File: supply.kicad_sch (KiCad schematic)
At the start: 149 parts, among them IC1 TPS54561, J3 DC_SOCKET, J8 61300311121, Q11 DTC014TEBTL, Q12 DTC014TEBTL, Q13 DTC014TEBTL, U10 LM3881MME_NOPB, U12 AP62301WU-7, U17 SN74LVC1G07DBVRG4, U18 MAX812REUS+T, U19 PAC1954T-E/4MX, U2 TPS65295RJET, U20 PAC1954T-E/4MX, U21 SN74LVC1G07DBVRG4, U22 SN74LVC1G07DBVRG4, U4 AP62301WU-7, U5 AP62301WU-7, U9 AP62301WU-7

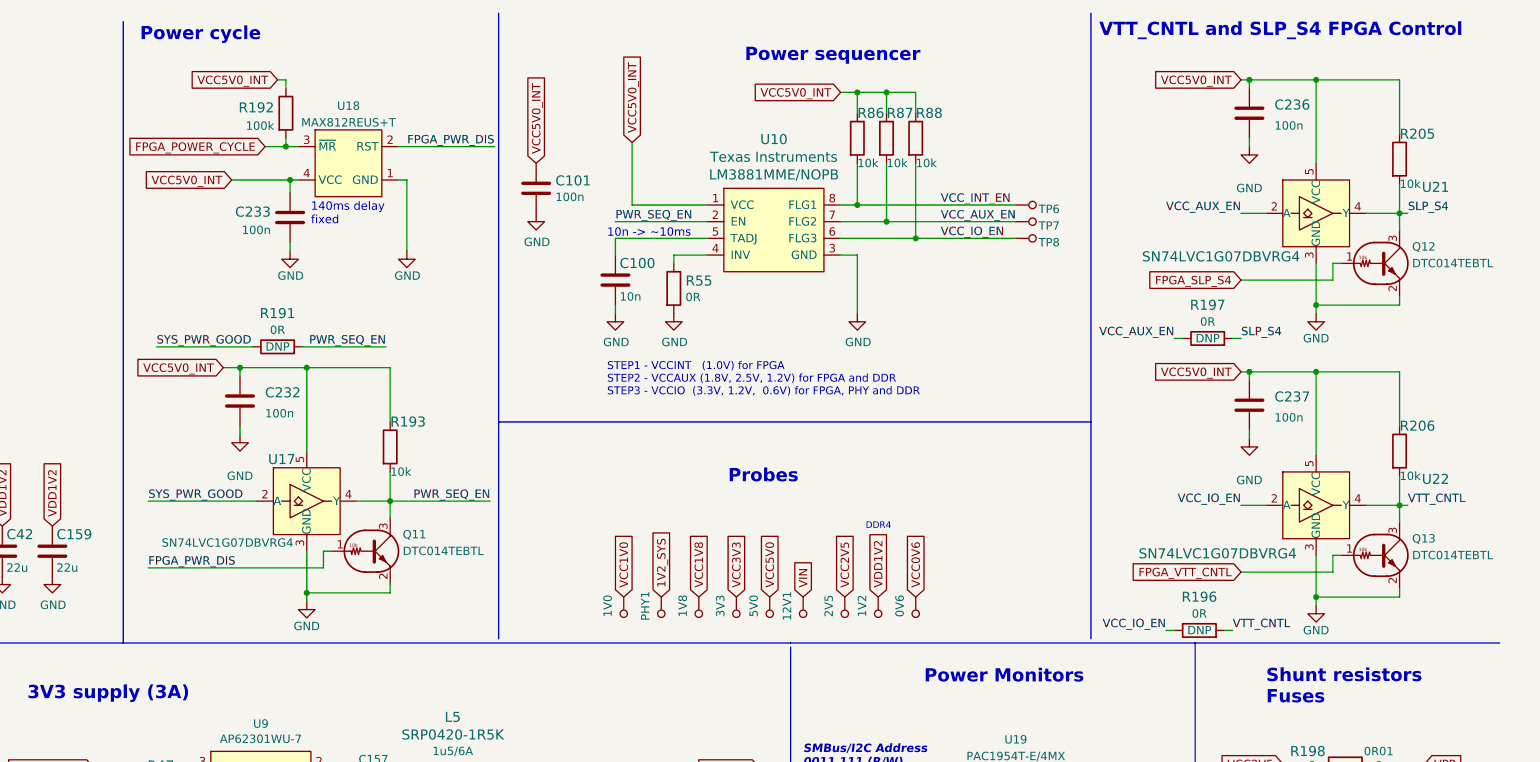
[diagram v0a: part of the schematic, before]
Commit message: Replace MODE2 jumpers with SMD DIP switch. Replace power cycle,VTT_CNTL and SLP_S4 ccircuits with tri-state buffer ones. Add possibilty to swith ETH paths with FPGA
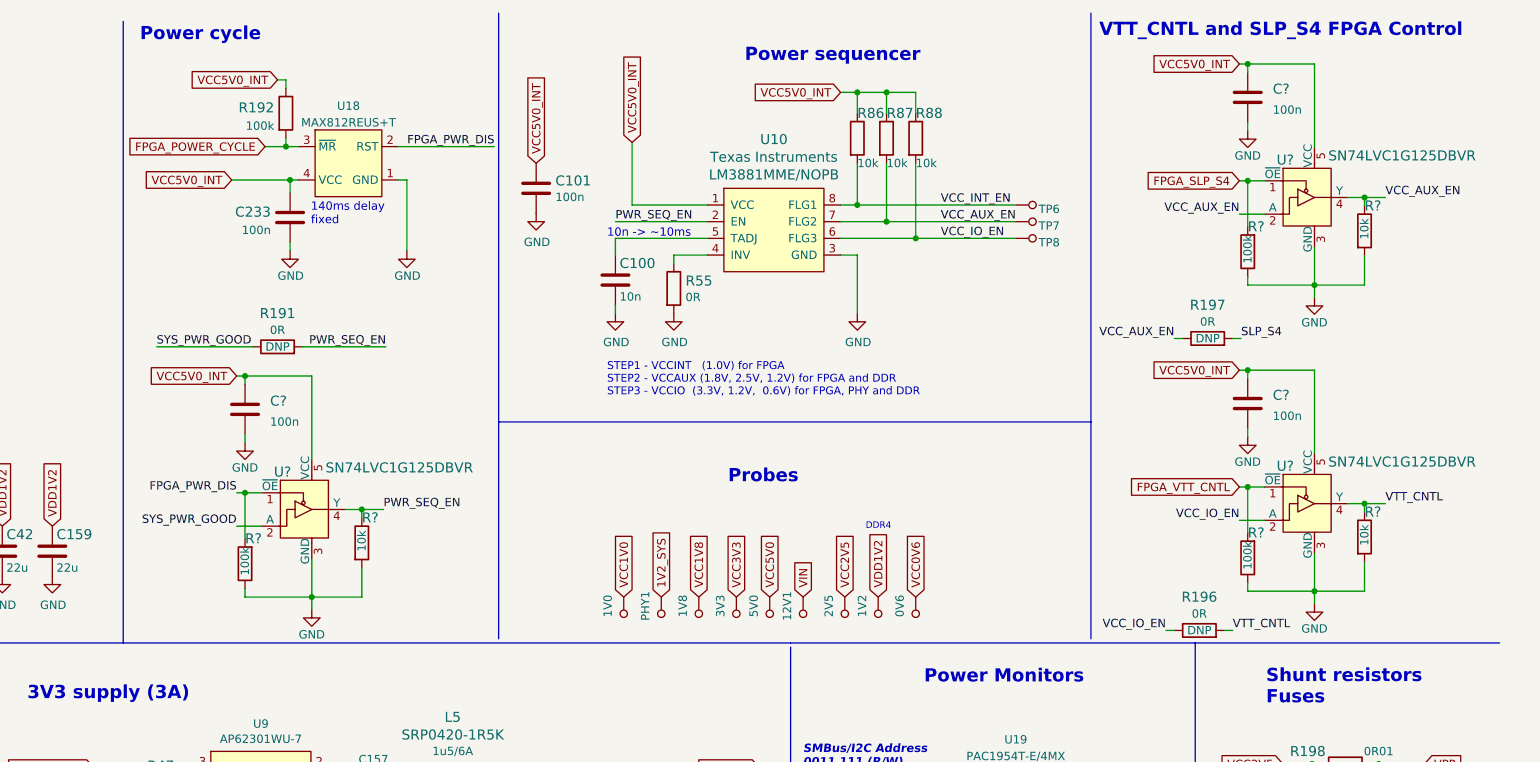
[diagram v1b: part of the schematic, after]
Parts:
- removed C232, C236, C237: C_100n_0402, antmicro-footprints:0402-cap, symbol antmicroCapacitors0402:C_100n_0402
- removed Q11, Q12, Q13: DTC014TEBTL, antmicro-footprints:SOT-416, symbol antmicroTransistorsBipolarSingle:DTC014TEBTL
- removed R193, R205, R206: R_10k_0402, data-center-dram-tester-footprints:0402-res, symbol data-center-dram-tester:R_10k_0402
- removed U17, U21, U22: SN74LVC1G07DBVRG4, antmicro-footprints:SOT-753, symbol antmicroLogicBuffersDriversReceiversTransceivers:SN74LVC1G07DBVRG4
- added C? (x3): C_100n_0402, antmicro-footprints:0402-cap, symbol antmicroCapacitors0402:C_100n_0402
- added R? (x3): R_10k_0402, data-center-dram-tester-footprints:0402-res, symbol data-center-dram-tester:R_10k_0402
- added R? (x3): R_100k_0402, data-center-dram-tester-footprints:0402-res, symbol data-center-dram-tester:R_100k_0402
- added U? (x3): SN74LVC1G125DBVR, antmicro-footprints:SOT-753, symbol antmicroLogicBuffersDriversReceiversTransceivers:SN74LVC1G125DBVR
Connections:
- net FPGA_PWR_DIS: now also R?.2, U?.1 (~{OE})
- net FPGA_SLP_S4: now also R?.2, U?.1 (~{OE})
- net FPGA_VTT_CNTL: now also R?.2, U?.1 (~{OE})
- net GND: now also C?.2, C?.2, C?.2, R?.1, R?.1, R?.1, R?.2, R?.2, R?.2, U?.3 (GND), U?.3 (GND), U?.3 (GND)
- net PWR_SEQ_EN: now also R?.1, U?.4 (Y)
- net SYS_PWR_GOOD: now also U?.2 (A)
- net VCC5V0: now also C?.1, C?.1, C?.1, U?.5 (VCC), U?.5 (VCC), U?.5 (VCC)
- net VCC_AUX_EN: now also R?.1, U?.2 (A), U?.4 (Y)
- net VCC_IO_EN: now also U?.2 (A)
- net VTT_CNTL: now also R?.1, U?.4 (Y)

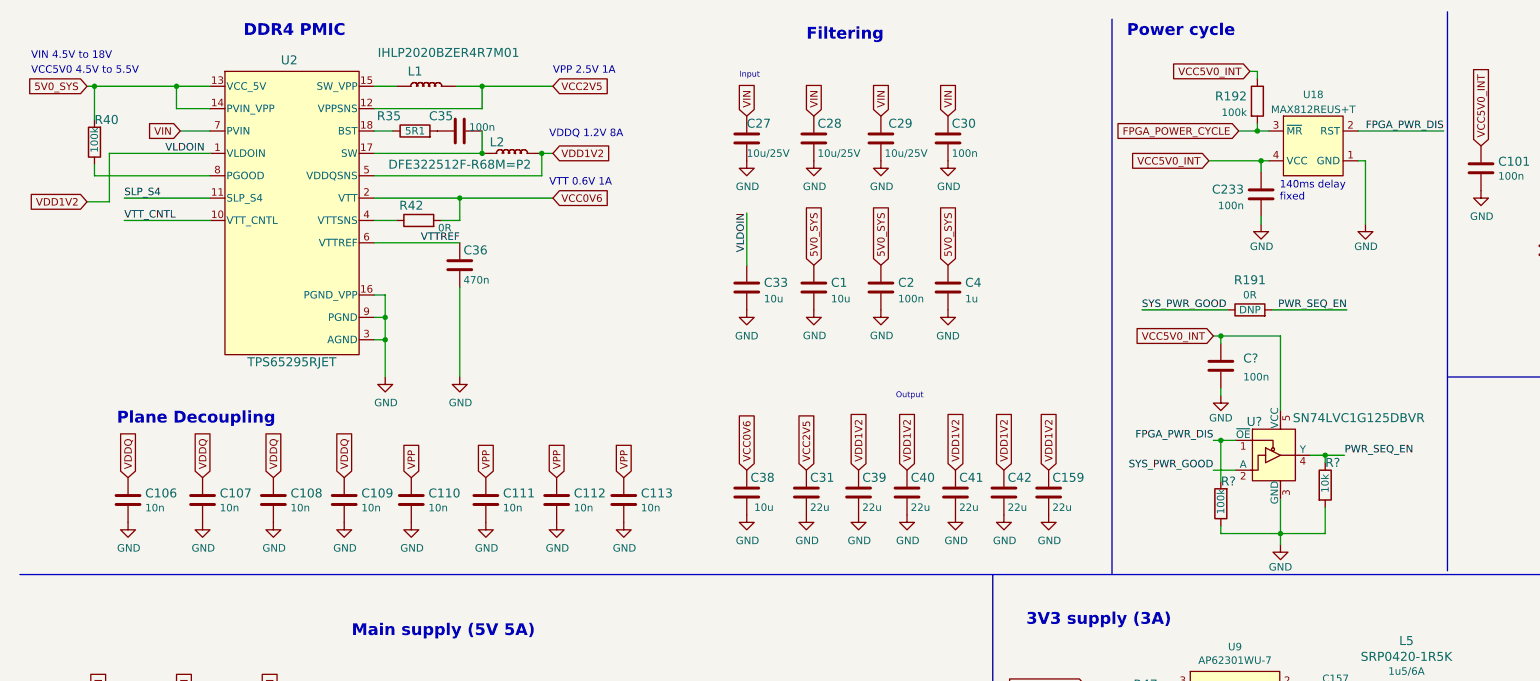
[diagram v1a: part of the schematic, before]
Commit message: Re-add mounting holes, add tri-state buffer for FPGA_POWER_CYCLE signal
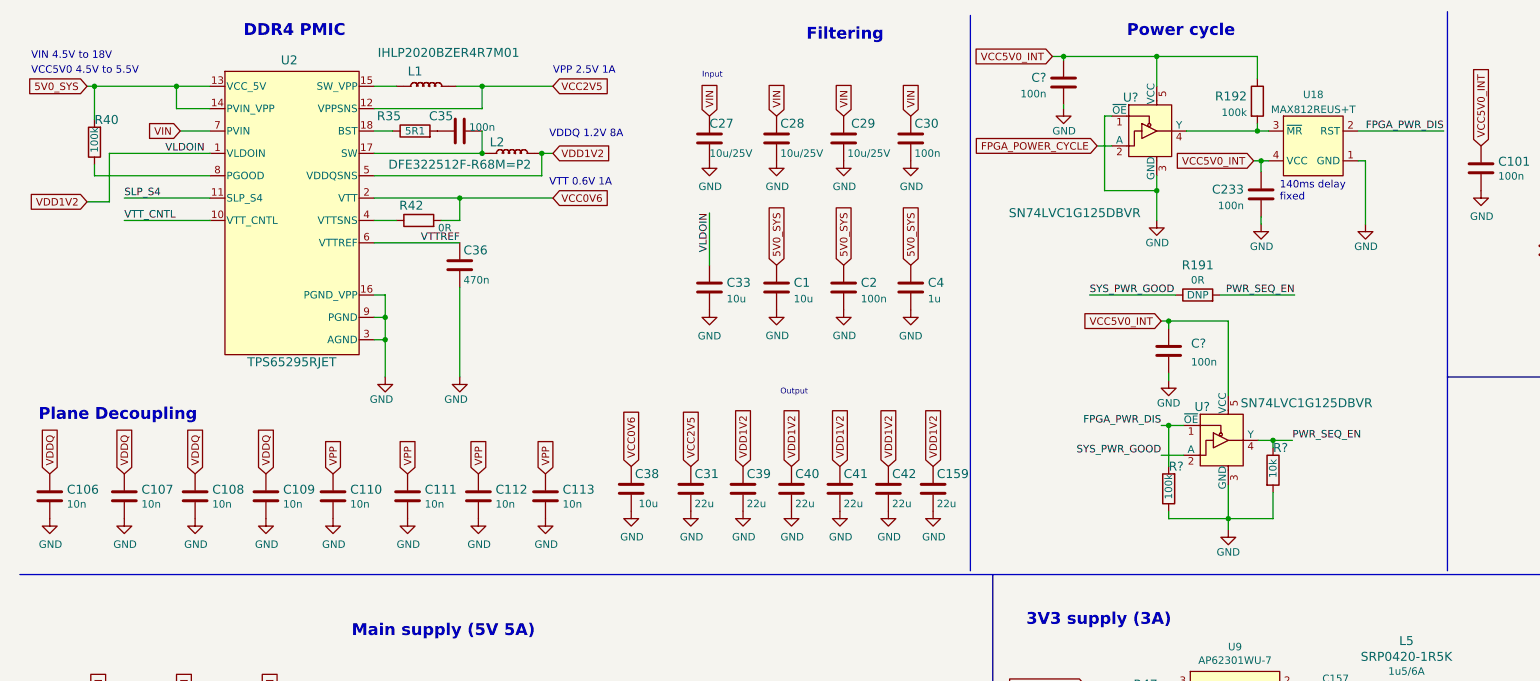
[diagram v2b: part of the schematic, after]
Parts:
- added C?: C_100n_0402, antmicro-footprints:0402-cap, symbol antmicroCapacitors0402:C_100n_0402
- added U?: SN74LVC1G125DBVR, antmicro-footprints:SOT-753, symbol antmicroLogicBuffersDriversReceiversTransceivers:SN74LVC1G125DBVR
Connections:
- net FPGA_POWER_CYCLE: now also U?.2 (A); no longer R192.2, U18.3 (~{MR})
- net GND: now also C?.2, U?.1 (~{OE}), U?.3 (GND)
- net VCC5V0: now also C?.1, U?.5 (VCC)
- new net: R192.2, U18.3 (~{MR}), U?.4 (Y)
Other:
- moved on the sheet: C1, C106, C107, C108, C109, C110, C111, C112, C113, C159, C2, C27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

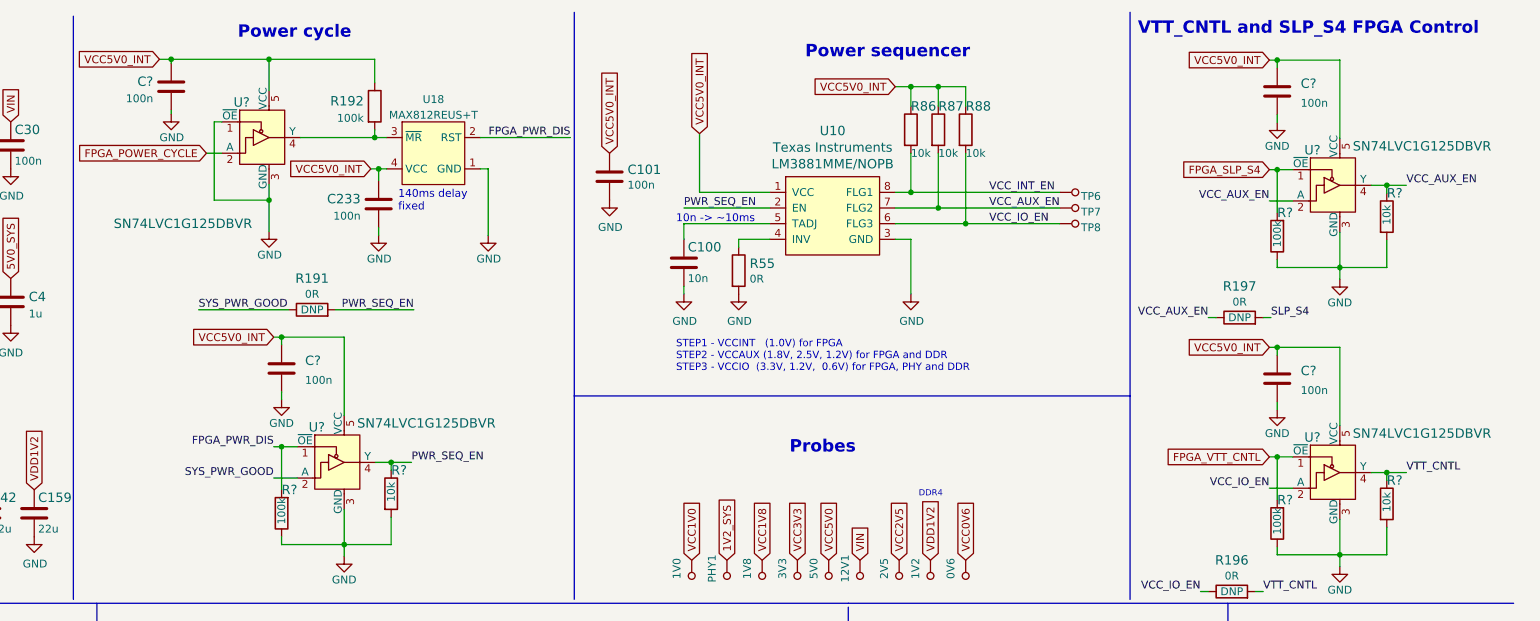
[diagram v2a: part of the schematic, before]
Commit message: Correct PCIe pin assigment, replace MODE2 symbol, export changes to PCB, progess in the new components placement
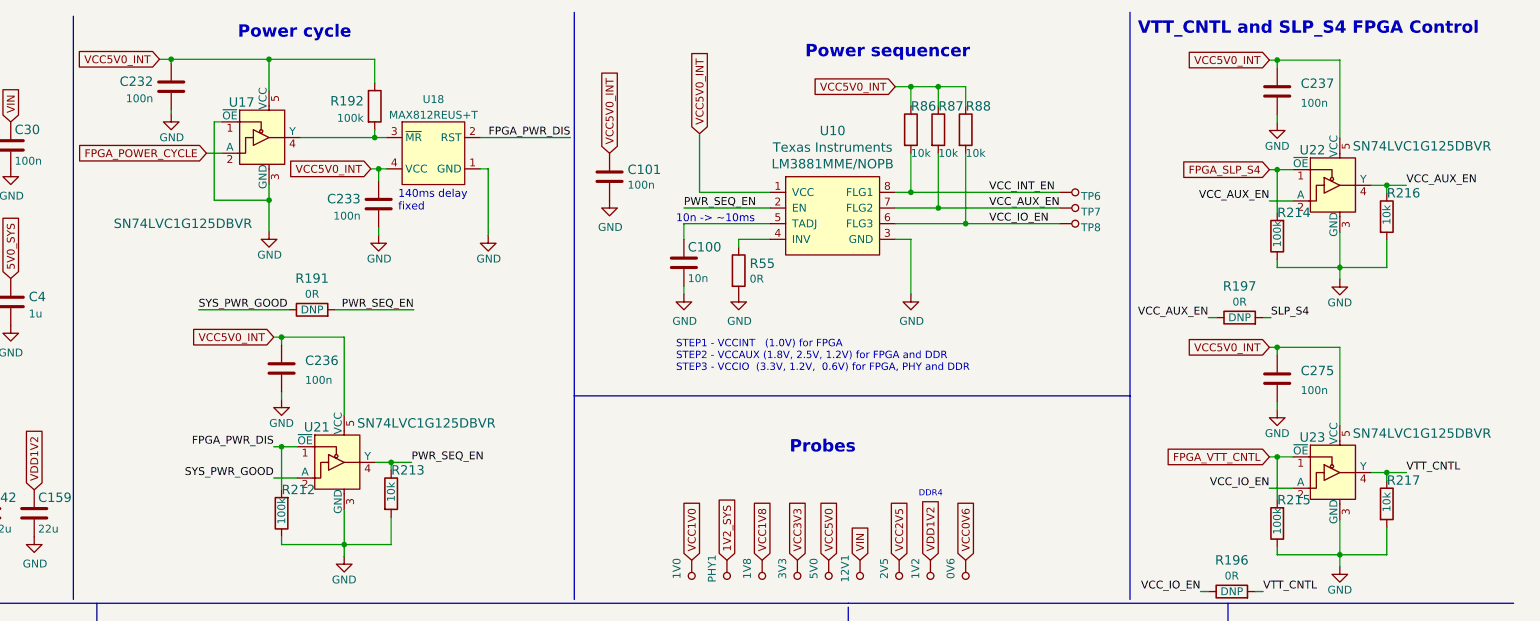
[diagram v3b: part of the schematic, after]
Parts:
- gave numbers to parts that had none: 14
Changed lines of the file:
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@@
   (symbol (lib_id "antmicroLogicBuffersDriversReceiversTransceivers:SN74LVC1G125DBVR") (at 217.932 85.725 0) (unit 1)
     (in_bom yes) (on_board yes)
-    (property "Reference" "U?" (id 0) (at 213.487 80.01 0)
+    (property "Reference" "U21" (id 0) (at 213.487 80.01 0)
       (effects (font (size 1.524 1.524)))
     )
@@
   (symbol (lib_id "power:GND") (at 217.932 100.965 0) (unit 1)
     (in_bom yes) (on_board yes)
-    (property "Reference" "#PWR?" (id 0) (at 217.932 107.315 0)
+    (property "Reference" "#PWR0334" (id 0) (at 217.932 107.315 0)
       (effects (font (size 1.27 1.27)) hide)
     )
@@
   (symbol (lib_id "antmicroLogicBuffersDriversReceiversTransceivers:SN74LVC1G125DBVR") (at 205.74 33.02 0) (unit 1)
     (in_bom yes) (on_board yes)
-    (property "Reference" "U?" (id 0) (at 201.295 27.305 0)
+    (property "Reference" "U17" (id 0) (at 201.295 27.305 0)
       (effects (font (size 1.524 1.524)))
     )
@@
   (symbol (lib_id "antmicroCapacitors0402:C_100n_0402") (at 189.865 24.765 0) (unit 1)
     (in_bom yes) (on_board yes) (fields_autoplaced)
-    (property "Reference" "C?" (id 0) (at 186.944 23.9304 0)
+    (property "Reference" "C232" (id 0) (at 186.944 23.9304 0)
       (effects (font (size 1.524 1.524)) (justify right))
     )
@@
   (symbol (lib_id "data-center-dram-tester:R_10k_0402") (at 387.096 92.456 270) (unit 1)
     (in_bom yes) (on_board yes)
-    (property "Reference" "R?" (id 0) (at 387.096 88.646 90)
+    (property "Reference" "R217" (id 0) (at 387.096 88.646 90)
       (effects (font (size 1.524 1.524)) (justify left))
     )
@@
   (symbol (lib_id "power:GND") (at 379.476 56.007 0) (unit 1)
     (in_bom yes) (on_board yes)
-    (property "Reference" "#PWR?" (id 0) (at 379.476 62.357 0)
+    (property "Reference" "#PWR0355" (id 0) (at 379.476 62.357 0)
       (effects (font (size 1.27 1.27)) hide)
     )
@@
   (symbol (lib_id "data-center-dram-tester:R_10k_0402") (at 225.552 90.805 270) (unit 1)
     (in_bom yes) (on_board yes)
-    (property "Reference" "R?" (id 0) (at 225.552 86.995 90)
+    (property "Reference" "R213" (id 0) (at 225.552 86.995 90)
       (effects (font (size 1.524 1.524)) (justify left))
     )
@@
   (symbol (lib_id "power:GND") (at 205.74 48.26 0) (unit 1)
     (in_bom yes) (on_board yes)
-    (property "Reference" "#PWR?" (id 0) (at 205.74 54.61 0)
+    (property "Reference" "#PWR0327" (id 0) (at 205.74 54.61 0)
       (effects (font (size 1.27 1.27)) hide)
     )
@@
   (symbol (lib_id "power:GND") (at 369.316 77.216 0) (unit 1)
     (in_bom yes) (on_board yes)
-    (property "Reference" "#PWR?" (id 0) (at 369.316 83.566 0)
+    (property "Reference" "#PWR0329" (id 0) (at 369.316 83.566 0)
       (effects (font (size 1.27 1.27)) hide)
     )
@@
   (symbol (lib_id "power:GND") (at 207.772 75.565 0) (unit 1)
     (in_bom yes) (on_board yes)
-    (property "Reference" "#PWR?" (id 0) (at 207.772 81.915 0)
+    (property "Reference" "#PWR0331" (id 0) (at 207.772 81.915 0)
       (effects (font (size 1.27 1.27)) hide)
     )
@@
   (symbol (lib_id "data-center-dram-tester:R_100k_0402") (at 207.772 93.98 90) (unit 1)
     (in_bom yes) (on_board yes)
-    (property "Reference" "R?" (id 0) (at 207.772 90.17 90)
+    (property "Reference" "R212" (id 0) (at 207.772 90.17 90)
       (effects (font (size 1.524 1.524)) (justify right))
     )
@@
   (symbol (lib_id "antmicroCapacitors0402:C_100n_0402") (at 369.316 72.136 0) (unit 1)
     (in_bom yes) (on_board yes)
-    (property "Reference" "C?" (id 0) (at 373.126 70.866 0)
+    (property "Reference" "C275" (id 0) (at 373.126 70.866 0)
       (effects (font (size 1.524 1.524)) (justify left))
     )
@@
   (symbol (lib_id "data-center-dram-tester:R_100k_0402") (at 369.316 95.631 90) (unit 1)
     (in_bom yes) (on_board yes)
-    (property "Reference" "R?" (id 0) (at 369.316 91.821 90)
+    (property "Reference" "R215" (id 0) (at 369.316 91.821 90)
       (effects (font (size 1.524 1.524)) (justify right))
     )
@@
   (symbol (lib_id "data-center-dram-tester:R_100k_0402") (at 369.316 49.022 90) (unit 1)
     (in_bom yes) (on_board yes)
-    (property "Reference" "R?" (id 0) (at 369.316 45.212 90)
+    (property "Reference" "R214" (id 0) (at 369.316 45.212 90)
       (effects (font (size 1.524 1.524)) (justify right))
     )
@@
   (symbol (lib_id "antmicroCapacitors0402:C_100n_0402") (at 207.772 70.485 0) (unit 1)
     (in_bom yes) (on_board yes)
-    (property "Reference" "C?" (id 0) (at 211.582 69.215 0)
+    (property "Reference" "C236" (id 0) (at 211.582 69.215 0)
       (effects (font (size 1.524 1.524)) (justify left))
     )
@@
   (symbol (lib_id "power:GND") (at 379.476 102.616 0) (unit 1)
     (in_bom yes) (on_board yes)
-    (property "Reference" "#PWR?" (id 0) (at 379.476 108.966 0)
+    (property "Reference" "#PWR0356" (id 0) (at 379.476 108.966 0)
       (effects (font (size 1.27 1.27)) hide)
     )
@@
   (symbol (lib_id "data-center-dram-tester:R_10k_0402") (at 387.096 45.847 270) (unit 1)
     (in_bom yes) (on_board yes)
-    (property "Reference" "R?" (id 0) (at 387.096 42.037 90)
+    (property "Reference" "R216" (id 0) (at 387.096 42.037 90)
       (effects (font (size 1.524 1.524)) (justify left))
     )
@@
   (symbol (lib_id "antmicroLogicBuffersDriversReceiversTransceivers:SN74LVC1G125DBVR") (at 379.476 40.767 0) (unit 1)
     (in_bom yes) (on_board yes)
-    (property "Reference" "U?" (id 0) (at 375.031 35.052 0)
+    (property "Reference" "U22" (id 0) (at 375.031 35.052 0)
       (effects (font (size 1.524 1.524)))
     )
@@
   (symbol (lib_id "power:GND") (at 189.865 29.21 0) (unit 1)
     (in_bom yes) (on_board yes)
-    (property "Reference" "#PWR?" (id 0) (at 189.865 35.56 0)
+    (property "Reference" "#PWR0336" (id 0) (at 189.865 35.56 0)
       (effects (font (size 1.27 1.27)) hide)
     )
@@
   (symbol (lib_id "antmicroLogicBuffersDriversReceiversTransceivers:SN74LVC1G125DBVR") (at 379.476 87.376 0) (unit 1)
     (in_bom yes) (on_board yes)
-    (property "Reference" "U?" (id 0) (at 375.031 81.661 0)
+    (property "Reference" "U23" (id 0) (at 375.031 81.661 0)
       (effects (font (size 1.524 1.524)))
     )
@@
   (symbol (lib_id "antmicroCapacitors0402:C_100n_0402") (at 369.316 25.527 0) (unit 1)
     (in_bom yes) (on_board yes)
-    (property "Reference" "C?" (id 0) (at 373.126 24.257 0)
+    (property "Reference" "C237" (id 0) (at 373.126 24.257 0)
       (effects (font (size 1.524 1.524)) (justify left))
     )
@@
   (symbol (lib_id "power:GND") (at 369.316 30.607 0) (unit 1)
     (in_bom yes) (on_board yes)
-    (property "Reference" "#PWR?" (id 0) (at 369.316 36.957 0)
-      (effects (font (size 1.27 1.27)) hide)
-    )
+    (property "Reference" "#PWR0328" (id 0) (at 369.316 36.957 0)
+      (effects (font (size 1.27 1.27)) hide)
+    )
